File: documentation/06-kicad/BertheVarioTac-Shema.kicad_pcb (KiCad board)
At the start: 2 copper layers, 86 x 50 mm, 15 parts, among them CN1 Temperature and humidity inte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, P1 Power supply base, P3 Extended IO, P4 SPEAK, P5 10 k ohms, SW1 SW_DIP_x01

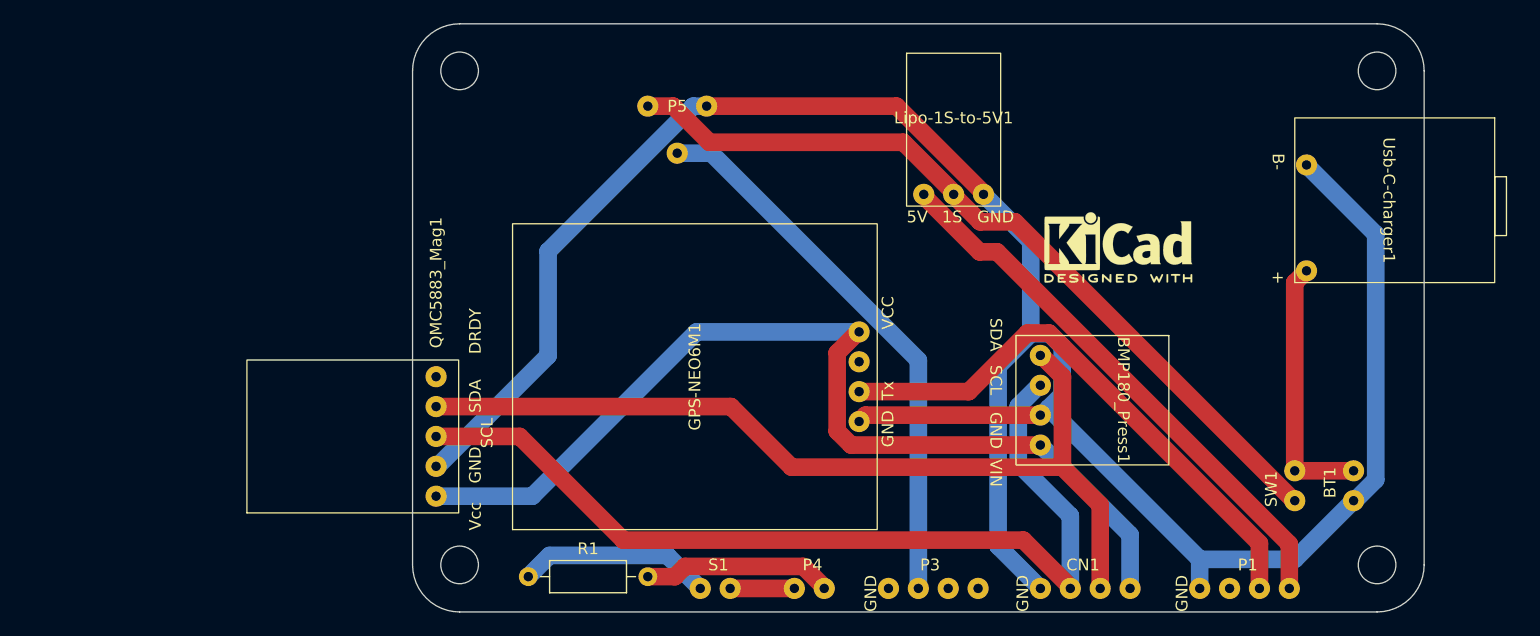
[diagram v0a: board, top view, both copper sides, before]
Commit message: pcb BMP180/MS5611 a tester
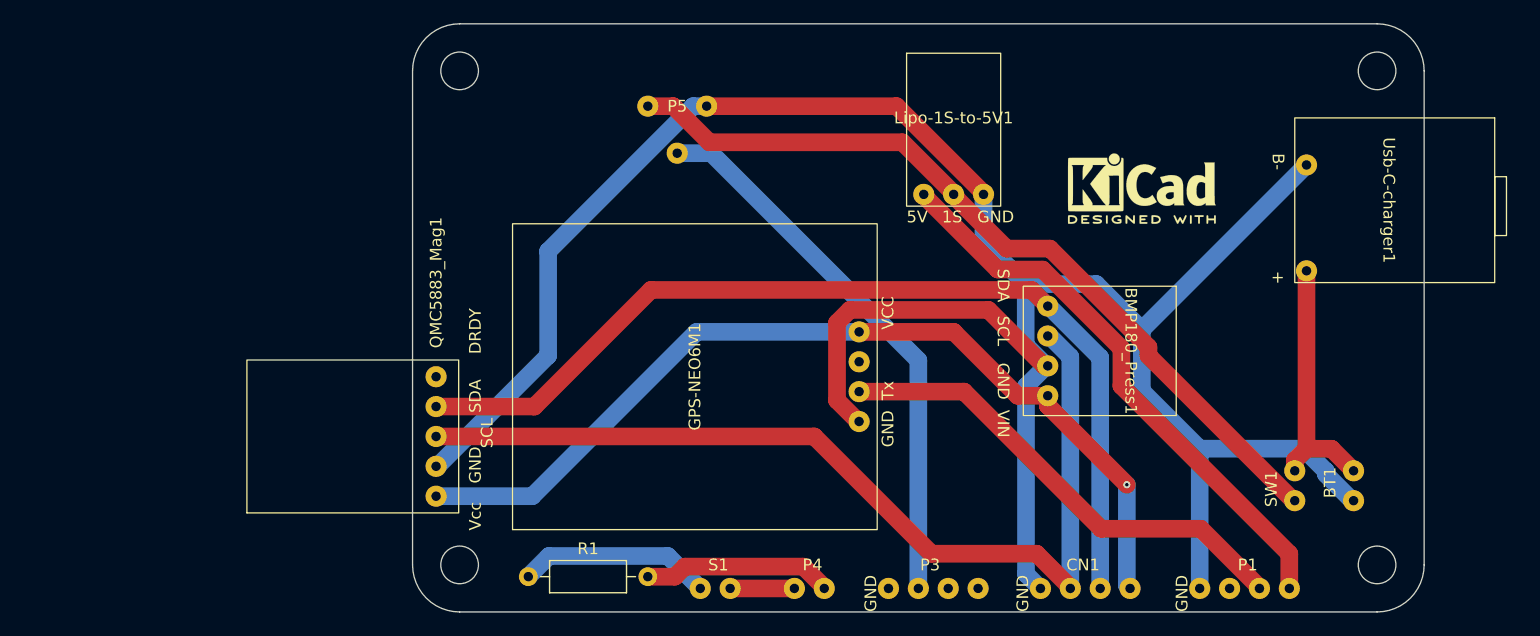
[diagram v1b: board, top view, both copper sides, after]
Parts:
- moved ESP32-2432S028_WROOM-32 5.39 mm to (154.0, 106.0)
- moved BMP180_Press1 4.24 mm to (147.5, 119.8)
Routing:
- net Net-(GPS-NEO6M1-TX): track 47.3 -> 41.0 mm
- net GNDREF: track 198.4 -> 204.6 mm
- net Net-(BMP180_Press1-SDA): track 77.3 -> 82.6 mm
- net Net-(BMP180_Press1-VIN): track 84.1 -> 79.3 mm, vias 0 -> 1
- net Net-(BMP180_Press1-SCL): track 79.3 -> 81.7 mm
- net Net-(Lipo-1S-to-5V1-OUT_5V): track 47.2 -> 48.6 mm

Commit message: modification pcb
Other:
- board text added: "3.3v"
- board text added: "IO22"
- board text added: "IO27"
- board text added: "IO35"
- board text added: "Tx"
- board text added: "Vin"
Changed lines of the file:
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@@
     (property "ki_keywords" "connector")
     (attr through_hole)
-    (fp_text reference "CN1" (at 2 -1.46 unlocked) (layer "F.SilkS")
+    (fp_text reference "CN1" (at 2.5 -6.96 unlocked) (layer "F.SilkS")
         (effects (font (size 1 1) (thickness 0.1)))
     )
@@
     (property "ki_keywords" "speaker sound")
     (attr through_hole)
-    (fp_text reference "S1" (at 2 -1 unlocked) (layer "F.SilkS")
+    (fp_text reference "S1" (at 2.5 -1 unlocked) (layer "F.SilkS")
         (effects (font (size 1 1) (thickness 0.1)))
     )
@@
     (property "ki_keywords" "connector")
     (attr through_hole)
-    (fp_text reference "P4" (at 2 -1 unlocked) (layer "F.SilkS")
+    (fp_text reference "P4" (at 2.5 -1 unlocked) (layer "F.SilkS")
         (effects (font (size 1 1) (thickness 0.1)))
     )
@@
         (effects (font (size 1 1) (thickness 0.15)))
     )
-    (fp_text user "VCC" (at 4 4.56 90 unlocked) (layer "F.SilkS")
+    (fp_text user "VCC" (at 3.5 5.06 90 unlocked) (layer "F.SilkS")
         (effects (font (size 1 1) (thickness 0.1)) (justify left bottom))
     )
@@
         (effects (font (size 1 1) (thickness 0.15)))
     )
-    (fp_text user "GND" (at -4 9 90 unlocked) (layer "F.SilkS")
+    (fp_text user "GND" (at -4.42 9 90 unlocked) (layer "F.SilkS")
         (effects (font (size 1 1) (thickness 0.1)) (justify left bottom))
     )
-    (fp_text user "Vcc" (at -8 9 90 unlocked) (layer "F.SilkS")
+    (fp_text user "Vcc" (at -7.42 9 90 unlocked) (layer "F.SilkS")
         (effects (font (size 1 1) (thickness 0.1)) (justify left bottom))
     )
@@
         (effects (font (size 1 1) (thickness 0.1)) (justify left bottom))
     )
-    (fp_text user "DRDY" (at 7 9 90 unlocked) (layer "F.SilkS")
+    (fp_text user "DRDY" (at 5.58 9 90 unlocked) (layer "F.SilkS")
         (effects (font (size 1 1) (thickness 0.1)) (justify left bottom))
     )
@@
     (property "ki_keywords" "connector")
     (attr through_hole)
-    (fp_text reference "P1" (at 2 -1 unlocked) (layer "F.SilkS")
+    (fp_text reference "P1" (at 2.5 -7 unlocked) (layer "F.SilkS")
         (effects (font (size 1 1) (thickness 0.1)))
     )
@@
         (effects (font (size 1 1) (thickness 0.15)))
     )
-    (fp_text user "VIN" (at 5 5.898 -90 unlocked) (layer "F.SilkS")
+    (fp_text user "VIN" (at 3.69 5.898 -90 unlocked) (layer "F.SilkS")
         (effects (font (size 1 1) (thickness 0.1)) (justify left bottom))
     )
-    (fp_text user "SDA" (at -7 5.898 -90 unlocked) (layer "F.SilkS")
+    (fp_text user "SDA" (at -6.31 5.898 -90 unlocked) (layer "F.SilkS")
         (effects (font (size 1 1) (thickness 0.1)) (justify left bottom))
     )
-    (fp_text user "GND" (at 1 5.898 -90 unlocked) (layer "F.SilkS")
+    (fp_text user "GND" (at 0.19 5.898 -90 unlocked) (layer "F.SilkS")
         (effects (font (size 1 1) (thickness 0.1)) (justify left bottom))
     )
@@
     (property "ki_keywords" "connector")
     (attr through_hole)
-    (fp_text reference "P3" (at 2 -1.54 unlocked) (layer "F.SilkS")
+    (fp_text reference "P3" (at 2.5 -6.04 unlocked) (layer "F.SilkS")
         (effects (font (size 1 1) (thickness 0.1)))
     )
@@
   (gr_line (start 178 96) (end 178 138)
     (stroke (width 0.05) (type default)) (layer "Edge.Cuts"))
+  (gr_text "IO27" (at 151 138.5 90) (layer "F.SilkS")
+    (effects (font (size 1 1) (thickness 0.1)) (justify left bottom))
+  )
+  (gr_text "Vin" (at 167 138.5 90) (layer "F.SilkS")
+    (effects (font (size 1 1) (thickness 0.1)) (justify left bottom))
+  )
+  (gr_text "Tx" (at 164.5 138.5 90) (layer "F.SilkS")
+    (effects (font (size 1 1) (thickness 0.1)) (justify left bottom))
+  )
+  (gr_text "IO22" (at 148.5 138.5 90) (layer "F.SilkS")
+    (effects (font (size 1 1) (thickness 0.1)) (justify left bottom))
+  )
+  (gr_text "3.3v" (at 153.5 138.5 90) (layer "F.SilkS")
+    (effects (font (size 1 1) (thickness 0.1)) (justify left bottom))
+  )
+  (gr_text "IO35" (at 135.5 138.5 90) (layer "F.SilkS")
+    (effects (font (size 1 1) (thickness 0.1)) (justify left bottom))
+  )
   (segment (start 101.84 139) (end 103.5974 137.2426) (width 1.5) (layer "B.Cu") (net 1))
   (segment (start 113.7026 137.2426) (end 116.46 140) (width 1.5) (layer "B.Cu") (net 1))

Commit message: modif pcb
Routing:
- net GNDREF: track 204.6 -> 0.00 mm
- net Net-(Lipo-1S-to-5V1-OUT_5V): track 48.6 -> 56.1 mm
- net Net-(BMP180_Press1-SDA): track 82.6 -> 81.4 mm
- net Net-(BMP180_Press1-VIN): track 79.3 -> 79.7 mm, vias 1 -> 0
- net Net-(GPS-NEO6M1-TX): vias 0 -> 1
- added copper zone on B.Cu, net GNDREF
- added copper zone on F.Cu, net GNDREF
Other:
- board text added: "bat +"
- board text added: "bat -"

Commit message: modif pcb
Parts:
- moved BMP180_Press1 6.00 mm to (147.5, 125.8)
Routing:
- net Net-(BMP180_Press1-VIN): track 79.7 -> 108.1 mm
- net Net-(BMP180_Press1-SCL): track 81.6 -> 71.3 mm
- net Net-(Lipo-1S-to-5V1-OUT_5V): track 56.1 -> 46.4 mm
- net Net-(BMP180_Press1-SDA): track 81.4 -> 75.5 mm
- net Net-(GPS-NEO6M1-TX): track 41.0 -> 45.1 mm, vias 1 -> 0

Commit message: modif pcb
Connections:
- Lipo-1S-to-5V1 pad 1: Net-(Lipo-1S-to-5V1-OUT_5V) -> GNDREF
- Lipo-1S-to-5V1 pad 3: GNDREF -> Net-(Lipo-1S-to-5V1-OUT_5V)
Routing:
- net Net-(Lipo-1S-to-5V1-OUT_5V): track 46.4 -> 44.3 mm
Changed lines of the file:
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@@
         (effects (font (size 1 1) (thickness 0.15)))
-    )
-    (fp_text user "GND" (at 2 6.5 unlocked) (layer "F.SilkS")
-        (effects (font (size 1 1) (thickness 0.1)) (justify left bottom))
-    )
-    (fp_text user "5V" (at -4 6.5 unlocked) (layer "F.SilkS")
-        (effects (font (size 1 1) (thickness 0.1)) (justify left bottom))
     )
     (fp_text user "1S" (at -1 6.5 unlocked) (layer "F.SilkS")
+        (effects (font (size 1 1) (thickness 0.1)) (justify left bottom))
+    )
+    (fp_text user "5V" (at 2 6.5 unlocked) (layer "F.SilkS")
+        (effects (font (size 1 1) (thickness 0.1)) (justify left bottom))
+    )
+    (fp_text user "GND" (at -4 6.5 unlocked) (layer "F.SilkS")
         (effects (font (size 1 1) (thickness 0.1)) (justify left bottom))
     )
@@
       (stroke (width 0.1) (type default)) (fill none) (layer "F.SilkS"))
     (pad "1" thru_hole circle (at -2.54 4) (size 1.8 1.8) (drill 0.8) (layers "*.Cu" "*.Mask")
-      (net 5 "Net-(Lipo-1S-to-5V1-OUT_5V)") (pinfunction "OUT_5V") (pintype "input"))
+      (net 4 "GNDREF") (pinfunction "GND") (pintype "input"))
     (pad "2" thru_hole circle (at 0 4) (size 1.8 1.8) (drill 0.8) (layers "*.Cu" "*.Mask")
       (net 17 "Net-(Lipo-1S-to-5V1-IN_3.7v)") (pinfunction "IN_3.7v") (pintype "input"))
     (pad "3" thru_hole circle (at 2.54 4) (size 1.8 1.8) (drill 0.8) (layers "*.Cu" "*.Mask")
-      (net 4 "GNDREF") (pinfunction "GND") (pintype "input"))
+      (net 5 "Net-(Lipo-1S-to-5V1-OUT_5V)") (pinfunction "OUT_5V") (pintype "input"))
   )
   (footprint "BertheShema:2 trous standard" (layer "F.Cu")
@@
     (effects (font (size 1 1) (thickness 0.1)) (justify left bottom))
   )
+  (segment (start 101.84 139) (end 103.6068 137.2332) (width 1.5) (layer "B.Cu") (net 1))
   (segment (start 103.6068 137.2332) (end 113.6932 137.2332) (width 1.5) (layer "B.Cu") (net 1))
   (segment (start 113.6932 137.2332) (end 116.46 140) (width 1.5) (layer "B.Cu") (net 1))
-  (segment (start 101.84 139) (end 103.6068 137.2332) (width 1.5) (layer "B.Cu") (net 1))
+  (segment (start 114.3 139) (end 115.2083 138.0917) (width 1.5) (layer "F.Cu") (net 2))
+  (segment (start 115.2083 138.0917) (end 125.2139 138.0917) (width 1.5) (layer "F.Cu") (net 2))
   (segment (start 127 139.8778) (end 127 140) (width 1.5) (layer "F.Cu") (net 2))
-  (segment (start 115.2083 138.0917) (end 125.2139 138.0917) (width 1.5) (layer "F.Cu") (net 2))
-  (segment (start 114.3 139) (end 115.2083 138.0917) (width 1.5) (layer "F.Cu") (net 2))
+  (segment (start 112 139) (end 114.3 139) (width 1.5) (layer "F.Cu") (net 2))
   (segment (start 125.2139 138.0917) (end 127 139.8778) (width 1.5) (layer "F.Cu") (net 2))
-  (segment (start 112 139) (end 114.3 139) (width 1.5) (layer "F.Cu") (net 2))
   (segment (start 172 130) (end 167 130) (width 1.5) (layer "F.Cu") (net 3))
   (segment (start 167 114) (end 167 130) (width 1.5) (layer "B.Cu") (net 3))
   (segment (start 168 113) (end 167 114) (width 1.5) (layer "B.Cu") (net 3))
-  (segment (start 166.54 137.7377) (end 166.54 140) (width 1.5) (layer "B.Cu") (net 5))
-  (segment (start 135.46 106.6577) (end 166.54 137.7377) (width 1.5) (layer "B.Cu") (net 5))
-  (segment (start 135.46 106.5) (end 135.46 106.6577) (width 1.5) (layer "B.Cu") (net 5))
-  (segment (start 164 137.3058) (end 146.8403 120.1461) (width 1.5) (layer "F.Cu") (net 6))
+  (segment (start 166.54 140) (end 166.54 137.5656) (width 1.5) (layer "B.Cu") (net 5))
+  (segment (start 166.54 137.5656) (end 140.54 111.5656) (width 1.5) (layer "B.Cu") (net 5))
+  (segment (start 140.54 111.5656) (end 140.54 106.5) (width 1.5) (layer "B.Cu") (net 5))
   (segment (start 146.8403 120.1461) (end 138.0178 120.1461) (width 1.5) (layer "F.Cu") (net 6))
-  (segment (start 138.0178 120.1461) (end 134.8939 123.27) (width 1.5) (layer "F.Cu") (net 6))
   (segment (start 134.8939 123.27) (end 129.964 123.27) (width 1.5) (layer "F.Cu") (net 6))
   (segment (start 164 140) (end 164 137.3058) (width 1.5) (layer "F.Cu") (net 6))
+  (segment (start 164 137.3058) (end 146.8403 120.1461) (width 1.5) (layer "F.Cu") (net 6))
+  (segment (start 138.0178 120.1461) (end 134.8939 123.27) (width 1.5) (layer "F.Cu") (net 6))
+  (segment (start 135 120.6009) (end 135 140) (width 1.5) (layer "B.Cu") (net 10))
   (segment (start 114.5 103) (end 117.3991 103) (width 1.5) (layer "B.Cu") (net 10))
-  (segment (start 135 120.6009) (end 135 140) (width 1.5) (layer "B.Cu") (net 10))
   (segment (start 117.3991 103) (end 135 120.6009) (width 1.5) (layer "B.Cu") (net 10))
   (segment (start 124.46 140) (end 119 140) (width 1.5) (layer "F.Cu") (net 12))
+  (segment (start 94 132.16) (end 143.46 132.16) (width 1.5) (layer "F.Cu") (net 14))
   (segment (start 143.46 132.16) (end 146 129.62) (width 1.5) (layer "F.Cu") (net 14))
-  (segment (start 94 132.16) (end 143.46 132.16) (width 1.5) (layer "F.Cu") (net 14))
+  (segment (start 153 136.62) (end 153 140) (width 1.5) (layer "B.Cu") (net 14))
+  (segment (start 108.0605 118.19) (end 129.964 118.19) (width 1.5) (layer "B.Cu") (net 14))
+  (segment (start 94.0905 132.16) (end 108.0605 118.19) (width 1.5) (layer "B.Cu") (net 14))
   (segment (start 146 129.62) (end 153 136.62) (width 1.5) (layer "B.Cu") (net 14))
-  (segment (start 94.0905 132.16) (end 108.0605 118.19) (width 1.5) (layer "B.Cu") (net 14))
   (segment (start 94 132.16) (end 94.0905 132.16) (width 1.5) (layer "B.Cu") (net 14))
-  (segment (start 108.0605 118.19) (end 129.964 118.19) (width 1.5) (layer "B.Cu") (net 14))
-  (segment (start 153 136.62) (end 153 140) (width 1.5) (layer "B.Cu") (net 14))
+  (segment (start 94 124.54) (end 123.8499 124.54) (width 1.5) (layer "F.Cu") (net 15))
   (segment (start 146.0911 122) (end 146 122) (width 1.5) (layer "F.Cu") (net 15))
+  (segment (start 126.9752 127.6653) (end 133.2993 127.6653) (width 1.5) (layer "F.Cu") (net 15))
   (segment (start 133.2993 127.6653) (end 138.9646 122) (width 1.5) (layer "F.Cu") (net 15))
+  (segment (start 150.46 126.3689) (end 146.0911 122) (width 1.5) (layer "F.Cu") (net 15))
   (segment (start 123.8499 124.54) (end 126.9752 127.6653) (width 1.5) (layer "F.Cu") (net 15))
-  (segment (start 126.9752 127.6653) (end 133.2993 127.6653) (width 1.5) (layer "F.Cu") (net 15))
+  (segment (start 138.9646 122) (end 146 122) (width 1.5) (layer "F.Cu") (net 15))
   (segment (start 150.46 140) (end 150.46 126.3689) (width 1.5) (layer "F.Cu") (net 15))
-  (segment (start 94 124.54) (end 123.8499 124.54) (width 1.5) (layer "F.Cu") (net 15))
-  (segment (start 150.46 126.3689) (end 146.0911 122) (width 1.5) (layer "F.Cu") (net 15))
-  (segment (start 138.9646 122) (end 146 122) (width 1.5) (layer "F.Cu") (net 15))
-  (segment (start 94 127.08) (end 121.7317 127.08) (width 1.5) (layer "F.Cu") (net 16))
+  (segment (start 110.8274 129.3815) (end 136.6845 129.3815) (width 1.5) (layer "F.Cu") (net 16))
   (segment (start 147.92 126.3374) (end 147.92 140) (width 1.5) (layer "F.Cu") (net 16))
   (segment (start 146.1226 124.54) (end 147.92 126.3374) (width 1.5) (layer "F.Cu") (net 16))
-  (segment (start 136.6545 129.4115) (end 141.526 124.54) (width 1.5) (layer "F.Cu") (net 16))
-  (segment (start 124.0632 129.4115) (end 136.6545 129.4115) (width 1.5) (layer "F.Cu") (net 16))
-  (segment (start 121.7317 127.08) (end 124.0632 129.4115) (width 1.5) (layer "F.Cu") (net 16))
   (segment (start 141.526 124.54) (end 146 124.54) (width 1.5) (layer "F.Cu") (net 16))
+  (segment (start 108.5259 127.08) (end 110.8274 129.3815) (width 1.5) (layer "F.Cu") (net 16))
+  (segment (start 136.6845 129.3815) (end 141.526 124.54) (width 1.5) (layer "F.Cu") (net 16))
+  (segment (start 94 127.08) (end 108.5259 127.08) (width 1.5) (layer "F.Cu") (net 16))
   (segment (start 146 124.54) (end 146.1226 124.54) (width 1.5) (layer "F.Cu") (net 16))
-  (segment (start 132.5118 100.9245) (end 138 106.4127) (width 1.5) (layer "F.Cu") (net 17))
-  (segment (start 138 106.4127) (end 138 106.5) (width 1.5) (layer "F.Cu") (net 17))
-  (segment (start 112 99) (end 113.9245 100.9245) (width 1.5) (layer "F.Cu") (net 17))
-  (segment (start 113.9245 100.9245) (end 132.5118 100.9245) (width 1.5) (layer "F.Cu") (net 17))
-  (segment (start 163.9481 132.54) (end 167 132.54) (width 1.5) (layer "B.Cu") (net 17))
-  (segment (start 138 106.5) (end 138 106.5919) (width 1.5) (layer "B.Cu") (net 17))
-  (segment (start 138 106.5919) (end 163.9481 132.54) (width 1.5) (layer "B.Cu") (net 17))
+  (segment (start 167 132.54) (end 163.9559 132.54) (width 1.5) (layer "F.Cu") (net 17))
+  (segment (start 138 106.5841) (end 138 106.5) (width 1.5) (layer "F.Cu") (net 17))
+  (segment (start 163.9559 132.54) (end 138 106.5841) (width 1.5) (layer "F.Cu") (net 17))
+  (segment (start 112 99) (end 113.9245 100.9245) (width 1.5) (layer "B.Cu") (net 17))
+  (segment (start 138 106.4127) (end 138 106.5) (width 1.5) (layer "B.Cu") (net 17))
+  (segment (start 132.5118 100.9245) (end 138 106.4127) (width 1.5) (layer "B.Cu") (net 17))
+  (segment (start 113.9245 100.9245) (end 132.5118 100.9245) (width 1.5) (layer "B.Cu") (net 17))
   (zone (net 4) (net_name "GNDREF") (layer "F.Cu") (hatch edge 0.5)
     (connect_pads (clearance 0.5))

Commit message: modif pcb
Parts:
- moved GPS-NEO6M1 4.12 mm to (132.5, 122.8)
- moved BMP180_Press1 3.24 mm to (148.1, 129.0)
- moved QMC5883_Mag1 1.39 mm to (88.0, 128.1)
- moved Usb-C-charger1 1.28 mm to (175.8, 106.0)
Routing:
- net Net-(GPS-NEO6M1-TX): track 45.1 -> 36.7 mm
- net Net-(BMP180_Press1-SCL): track 71.3 -> 65.4 mm
- net Net-(BMP180_Press1-VIN): track 108.1 -> 106.0 mm
- net Net-(P3-Pin_3): track 47.2 -> 45.5 mm
- net Net-(BT1-+): track 22.4 -> 23.0 mm

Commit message: R sda scl pcb
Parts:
- added R2: 4.7k, BertheShema:R_47, F.Cu at (106.5, 99.0)
- added R3: 4.7k, BertheShema:R_47, F.Cu at (106.5, 103.5)
- moved P5 6.71 mm to (120.5, 96.5)
- moved Lipo-1S-to-5V1 5.10 mm to (133.0, 101.5)
- moved BMP180_Press1 1.72 mm to (146.4, 129.3)
- moved BT1 1.00 mm to (173.0, 130.0)
- moved SW1 1.00 mm to (168.0, 132.5)
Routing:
- net Net-(BMP180_Press1-SDA): track 75.4 -> 100.5 mm, vias 0 -> 1
- net Net-(BMP180_Press1-SCL): track 65.4 -> 90.2 mm
- net Net-(BMP180_Press1-VIN): track 106.0 -> 127.3 mm
- net Net-(Lipo-1S-to-5V1-IN_3.7v): track 69.0 -> 65.3 mm
- net Net-(Lipo-1S-to-5V1-OUT_5V): track 44.3 -> 47.3 mm
- net Net-(P3-Pin_3): track 45.5 -> 46.7 mm

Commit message: modification pcb
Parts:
- moved S1 49.5 mm to (168.5, 140.0)
- moved R1 42.1 mm to (143.9, 140.0)
- moved P4 34.5 mm to (161.5, 140.0)
- moved CN1 27.5 mm to (123.0, 140.0)
- moved P1 27.5 mm to (136.5, 140.0)
- moved P3 27.5 mm to (110.0, 140.0)
- moved Lipo-1S-to-5V1 1.14 mm to (132.5, 100.5)
- moved GPS-NEO6M1 1.12 mm to (132.0, 121.8)
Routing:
- net Net-(BMP180_Press1-VIN): track 127.3 -> 107.4 mm, vias 0 -> 1
- net Net-(BMP180_Press1-SDA): track 100.5 -> 89.9 mm, vias 1 -> 0
- net Net-(R1-Pad1): track 16.5 -> 25.0 mm
- net Net-(P4-Pin_1): track 16.2 -> 9.06 mm
- net Net-(P4-Pin_2): track 5.46 -> 11.2 mm
- net Net-(Lipo-1S-to-5V1-OUT_5V): track 47.3 -> 43.3 mm, vias 0 -> 1
- net Net-(GPS-NEO6M1-TX): track 37.1 -> 34.2 mm
- net Net-(BMP180_Press1-SCL): track 90.2 -> 87.7 mm
- net Net-(P3-Pin_3): track 46.7 -> 45.4 mm
